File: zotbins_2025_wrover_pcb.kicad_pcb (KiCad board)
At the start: 2 copper layers, 125 x 125 mm, 40 parts, among them J1 FFC2B28-24-G, J2 DCJ200-10-A-XX-K_REVA, J6 Conn_01x30_Pin, U2 MCP23017_SP, U3 XC6206P302MR-G, U4 XC6206P282PR-G, U5 LM7805_TO220, U6 ESP32-DEVKITC-32D

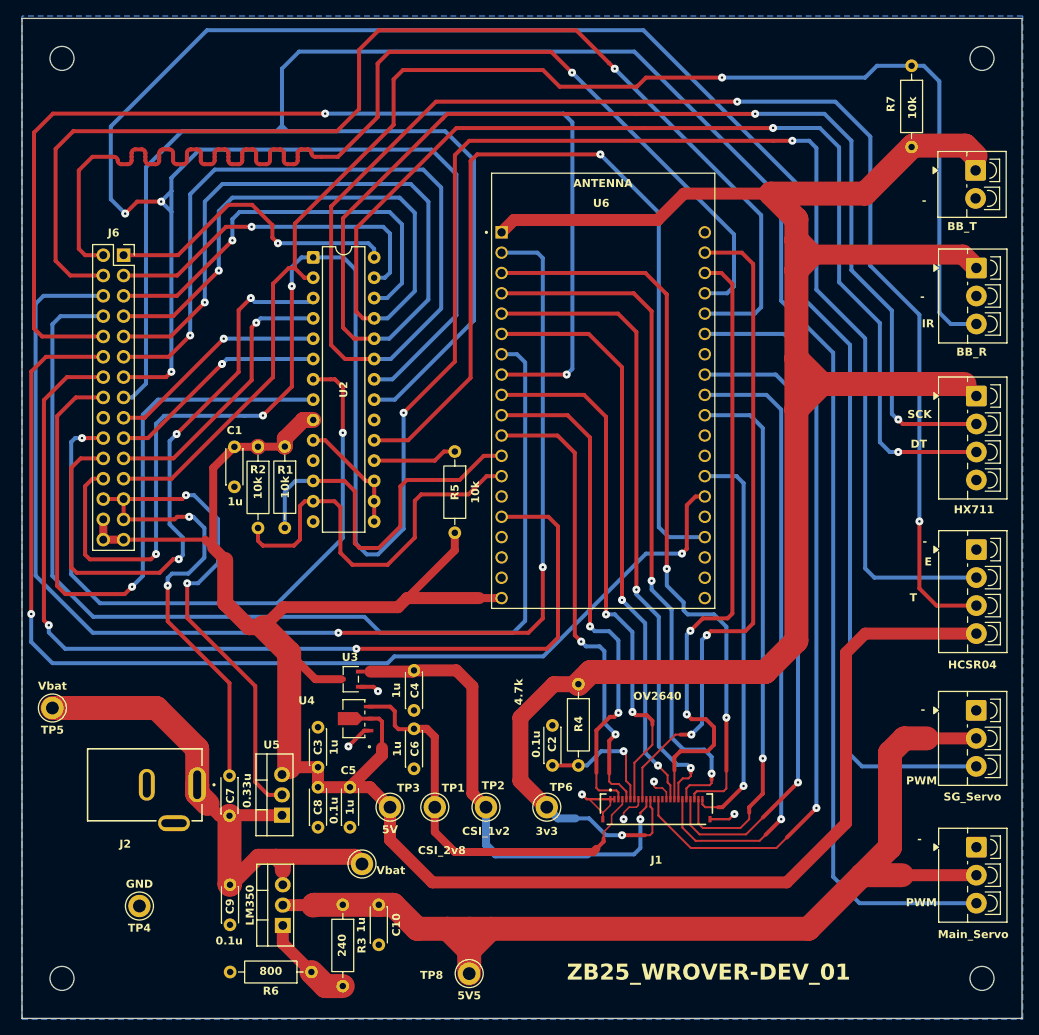
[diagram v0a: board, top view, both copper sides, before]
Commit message: hx711 bug update -- Digikey vendor sells different version of hx711 -> updated schematic + footprint
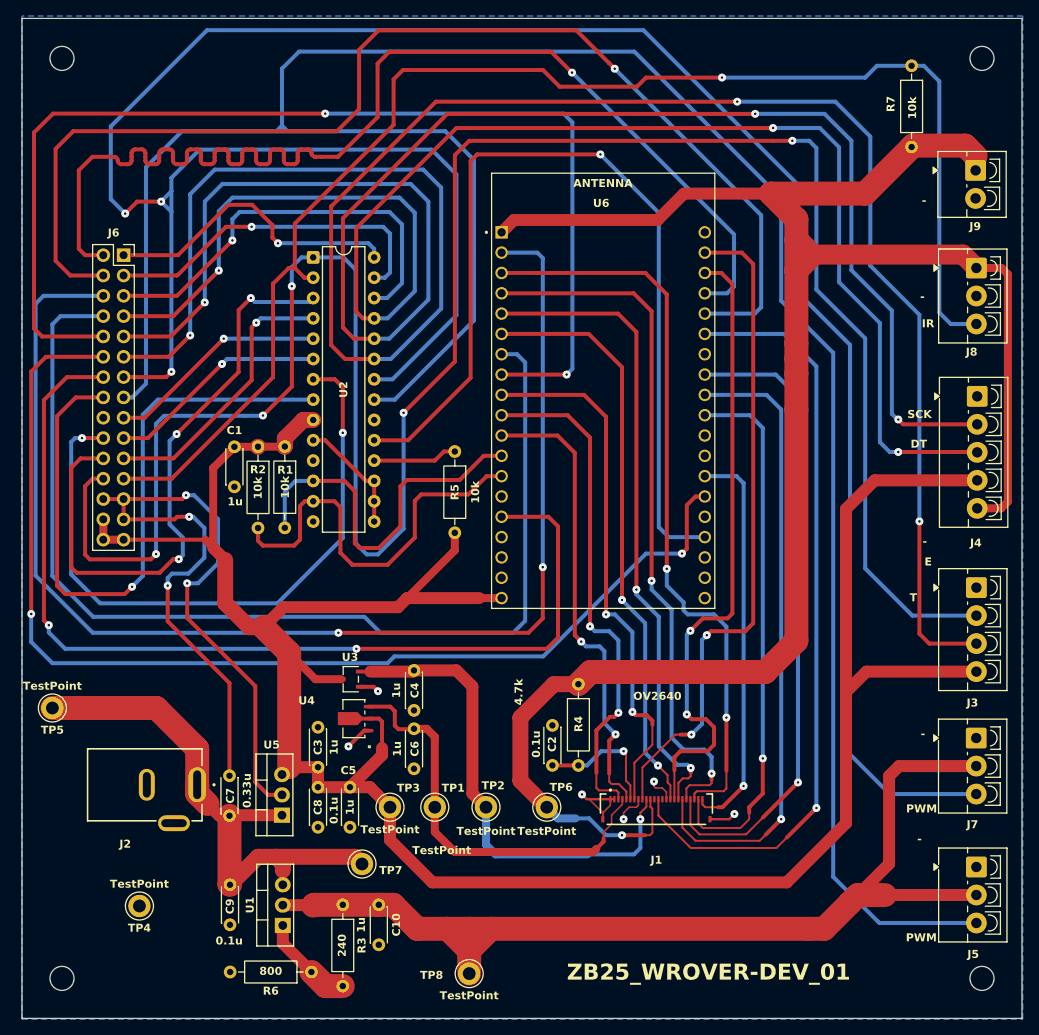
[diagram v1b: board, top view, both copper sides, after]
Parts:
- removed HX711: HX711_Screw_Terminal_01x04, TerminalBlock_4Ucon:TerminalBlock_4Ucon_1x04_P3.50mm_Vertical
- added J4: HX711_Screw_Terminal_01x05, TerminalBlock_4Ucon:TerminalBlock_4Ucon_1x05_P3.50mm_Vertical, F.Cu at (212.4, 84.6)
- TP1: value CSI_2v8 -> TestPoint
- TP2: value CSI_1v2 -> TestPoint
- TP3: value 5V -> TestPoint
- TP4: value GND -> TestPoint
- TP5: value Vbat -> TestPoint
- TP6: value 3v3 -> TestPoint
- TP8: value 5V5 -> TestPoint
- moved J3 4.75 mm to (212.3, 108.6)
- moved J7 3.46 mm to (212.3, 127.4)
- moved J5 2.48 mm to (212.3, 143.5)
- renumbered HCSR04 to J3, Main_Servo to J5, SG_Servo to J7, BB_R to J8, BB_T to J9, Vbat to TP7, LM350 to U1
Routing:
- net +5V: track 258.6 -> 294.5 mm
- net +3V3: track 249.1 -> 257.0 mm
- net /TRIG: track 251.7 -> 257.0 mm
- net /ECHO: track 287.1 -> 289.0 mm
- net /SG_SERVO_PWM: track 309.6 -> 311.0 mm
- net +5V5: track 132.2 -> 130.8 mm
- net /MAIN_SERVO_PWM: track 298.9 -> 300.0 mm

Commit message: completed PCB changes for iteration 2
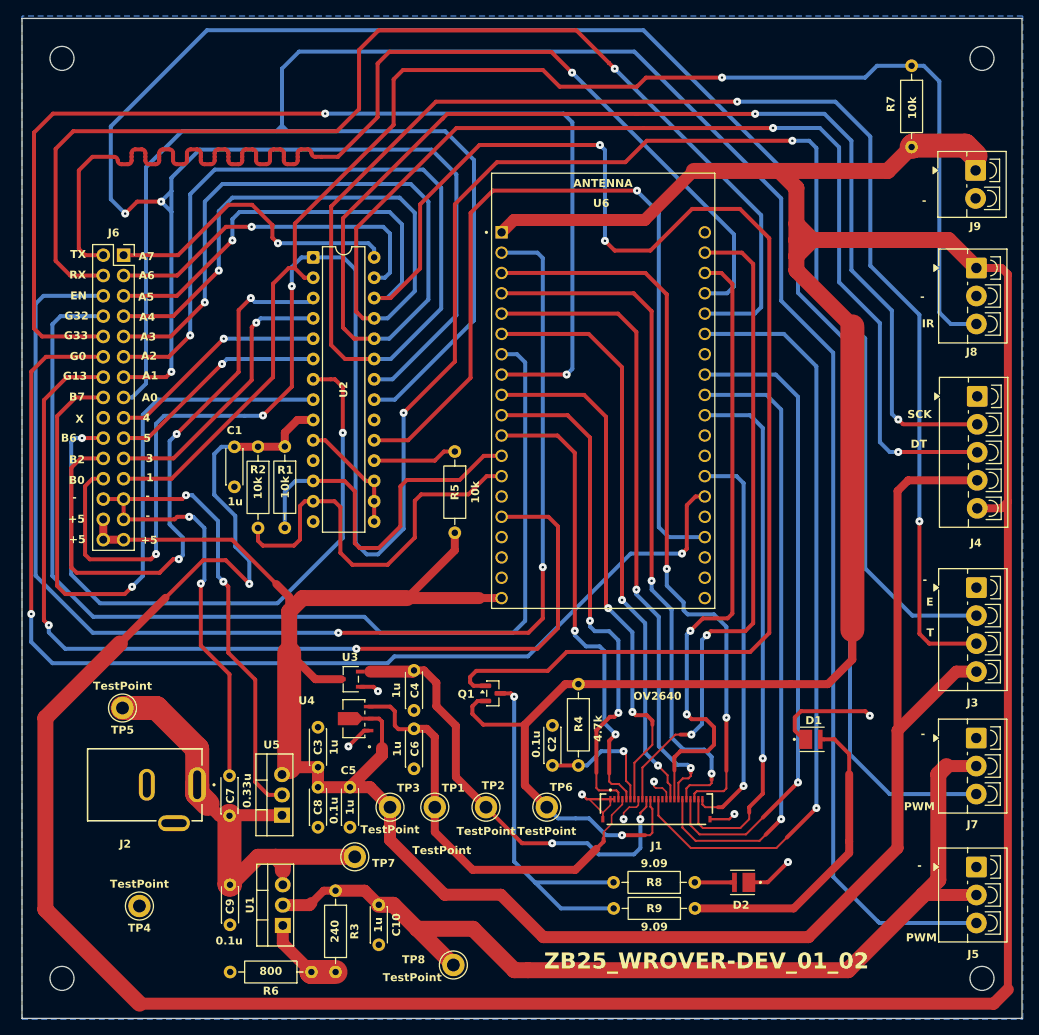
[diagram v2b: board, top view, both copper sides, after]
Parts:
- added D1: MP-3030-120H-30-95, LED:LED_MP-3030-120H-30-95, F.Cu at (191.8, 127.5)
- added D2: MP-3030-120H-30-95, LED:LED_MP-3030-120H-30-95, F.Cu at (183.1, 145.4)
- added Q1: IRLML9301, Package_TO_SOT_SMD:SOT-23, F.Cu at (151.9, 121.8)
- added R8: 9.09, Resistor_THT:R_Axial_DIN0207_L6.3mm_D2.5mm_P10.16mm_Horizontal, F.Cu at (177.1, 145.4)
- added R9: 9.09, Resistor_THT:R_Axial_DIN0207_L6.3mm_D2.5mm_P10.16mm_Horizontal, F.Cu at (177.1, 148.7)
- moved TP5 8.76 mm to (105.6, 123.6)
- moved TP8 2.25 mm to (146.9, 155.7)
- moved R3 1.98 mm to (132.2, 146.4)
- moved TP7 1.27 mm to (134.6, 142.2)
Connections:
- net /GPA5 renamed /~{LED}
- C1 pad 1: +5V -> +3V3
- R1 pad 1: +5V -> +3V3
- R2 pad 1: +5V -> +3V3
- U2 pad 9: +5V -> +3V3
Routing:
- net +3V3: track 257.0 -> 561.3 mm, vias 1 -> 2
- net /~{LED}: track 52.8 -> 222.4 mm, vias 1 -> 3
- net Net-(Q1-D): track 0.00 -> 47.2 mm, vias 0 -> 1
- net Net-(D1-PadA): track 0.00 -> 38.9 mm
- net +5V: track 294.5 -> 270.1 mm
- net GND: track 150.0 -> 160.6 mm, vias 10 -> 12
- net Net-(U1-VI): track 69.3 -> 59.3 mm
- net +5V5: track 130.8 -> 122.9 mm
- net /MCP_INTB: track 114.8 -> 107.3 mm
- net CSI_1V2: track 60.7 -> 55.6 mm, vias 1 -> 2
- net Net-(D2-PadA): track 0.00 -> 4.96 mm
- net /ECHO: track 289.0 -> 285.4 mm
- net CSI_2V8: track 51.3 -> 53.1 mm
- net Net-(U1-ADJ): track 12.0 -> 10.3 mm
- net /GPIO13: track 124.4 -> 123.7 mm
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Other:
- board text added: "ZB25_WROVER-DEV_01_02"
- board text removed: "V"
- board text removed: "ZB25_WROVER-DEV_01"

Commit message: minor adjustments + gerber files produced
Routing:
- net +3V3: track 561.3 -> 577.0 mm
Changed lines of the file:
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@@
 			(sketchdnponfab yes)
 			(crossoutdnponfab yes)
-			(subtractmaskfromsilk no)
+			(subtractmaskfromsilk yes)
 			(outputformat 1)
 			(mirror no)
@@
 	)
 	(segment
-		(start 131.642429 78.239717)
-		(end 131.642429 60.908968)
+		(start 205.179437 100.273394)
+		(end 205.179437 114.318387)
 		(width 0.5)
 		(layer "F.Cu")
@@
 	)
 	(segment
-		(start 205.179437 100.273394)
-		(end 205.179437 114.318387)
+		(start 205.179437 114.318387)
+		(end 206.412623 115.551573)
 		(width 0.5)
 		(layer "F.Cu")
@@
 	)
 	(segment
-		(start 131.642429 60.908968)
-		(end 144.741579 47.809818)
+		(start 133.377712 79.975)
+		(end 137.02 79.975)
 		(width 0.5)
 		(layer "F.Cu")
@@
 	)
 	(segment
-		(start 205.179437 114.318387)
-		(end 206.412623 115.551573)
+		(start 206.412623 115.551573)
+		(end 212.3 115.551573)
 		(width 0.5)
 		(layer "F.Cu")
@@
 	)
 	(segment
-		(start 144.741579 47.809818)
-		(end 182.405062 47.809818)
+		(start 114.025 77.025)
+		(end 111.35 79.7)
 		(width 0.5)
 		(layer "F.Cu")
@@
 	)
 	(segment
-		(start 206.412623 115.551573)
-		(end 212.3 115.551573)
+		(start 183.070342 47.809976)
+		(end 183.070184 47.809818)
 		(width 0.5)
 		(layer "F.Cu")
@@
 	)
 	(segment
-		(start 114.025 77.025)
-		(end 111.35 79.7)
+		(start 131.642429 60.908968)
+		(end 131.642429 78.239717)
 		(width 0.5)
 		(layer "F.Cu")
@@
 	)
 	(segment
-		(start 137.02 79.975)
-		(end 133.377712 79.975)
+		(start 183.070184 47.809818)
+		(end 144.741579 47.809818)
 		(width 0.5)
 		(layer "F.Cu")
@@
 	)
 	(segment
-		(start 133.377712 79.975)
-		(end 131.642429 78.239717)
+		(start 131.642429 78.239717)
+		(end 133.377712 79.975)
 		(width 0.5)
 		(layer "F.Cu")
@@
 		(net 25)
 	)
+	(segment
+		(start 144.741579 47.809818)
+		(end 131.642429 60.908968)
+		(width 0.5)
+		(layer "F.Cu")
+		(net 25)
+	)
 	(via
 		(at 205.177816 100.271773)
@@
 	)
 	(via
-		(at 182.405062 47.809818)
+		(at 183.070342 47.809976)
 		(size 1)
 		(drill 0.3)
@@
 	)
 	(segment
-		(start 182.405062 47.809818)
-		(end 194.675487 47.809818)
+		(start 199.04094 68.30805)
+		(end 205.177816 74.444926)
 		(width 0.5)
 		(layer "B.Cu")
@@
 	)
 	(segment
-		(start 194.675487 47.809818)
-		(end 199.04094 52.175271)
+		(start 205.177816 74.444926)
+		(end 205.177816 100.271773)
 		(width 0.5)
 		(layer "B.Cu")
@@
 	)
 	(segment
-		(start 199.04094 52.175271)
-		(end 199.04094 68.30805)
+		(start 143.15 56.3)
+		(end 145.4 58.55)
 		(width 0.5)
 		(layer "B.Cu")
@@
 	)
 	(segment
-		(start 143.15 56.3)
-		(end 145.4 58.55)
+		(start 114.025 77.025)
+		(end 114.025 59.375)
 		(width 0.5)
 		(layer "B.Cu")
@@
 	)
 	(segment
-		(start 114.025 77.025)
-		(end 114.025 59.375)
+		(start 194.675645 47.809976)
+		(end 199.04094 52.175271)
 		(width 0.5)
 		(layer "B.Cu")
@@
 	)
 	(segment
-		(start 199.04094 68.30805)
-		(end 205.177816 74.444926)
+		(start 183.070342 47.809976)
+		(end 194.675645 47.809976)
 		(width 0.5)
 		(layer "B.Cu")
@@
 	)
 	(segment
-		(start 205.177816 74.444926)
-		(end 205.177816 100.271773)
+		(start 199.04094 52.175271)
+		(end 199.04094 68.30805)
 		(width 0.5)
 		(layer "B.Cu")
@@
 	)
 	(segment
+		(start 189.291237 52.694359)
+		(end 171.097037 52.694359)
+		(width 0.5)
+		(layer "F.Cu")
+		(net 26)
+	)
+	(segment
 		(start 100.885425 95.868707)
 		(end 101.814132 94.94)
@@
 	)
 	(segment
-		(start 152.359682 55.377846)
-		(end 147.113266 60.624262)
+		(start 168.41355 55.377846)
+		(end 152.359682 55.377846)
 		(width 0.5)
 		(layer "F.Cu")
@@
 	)
 	(segment
-		(start 147.113266 80.286734)
-		(end 140.7 86.7)
+		(start 152.359682 55.377846)
+		(end 147.113266 60.624262)
 		(width 0.5)
 		(layer "F.Cu")
@@
 	)
 	(segment
+		(start 147.113266 60.624262)
+		(end 147.113266 80.286734)
+		(width 0.5)
+		(layer "F.Cu")
+		(net 26)
+	)
+	(segment
 		(start 126.733259 77.545184)
 		(end 126.733259 70.885526)
@@
 	)
 	(segment
-		(start 101.475983 105.017742)
-		(end 109.097872 105.017742)
+		(start 171.097037 52.694359)
+		(end 168.41355 55.377846)
 		(width 0.5)
 		(layer "F.Cu")
@@
 	)
 	(segment
-		(start 101.814132 94.94)
-		(end 103.16 94.94)
+		(start 101.475983 105.017742)
+		(end 109.097872 105.017742)
 		(width 0.5)
 		(layer "F.Cu")
@@
 	)
 	(segment
-		(start 171.097037 52.694359)
-		(end 168.41355 55.377846)
+		(start 101.814132 94.94)
+		(end 103.16 94.94)
 		(width 0.5)
 		(layer "F.Cu")
@@
 	)
 	(segment
-		(start 147.113266 60.624262)
-		(end 147.113266 80.286734)
+		(start 147.113266 80.286734)
+		(end 140.7 86.7)
 		(width 0.5)
 		(layer "F.Cu")
@@
 	)
 	(segment
-		(start 189.291237 52.694359)
-		(end 171.097037 52.694359)
-		(width 0.5)
-		(layer "F.Cu")
-		(net 26)
-	)
-	(segment
 		(start 126.733259 83.426723)
 		(end 126.733259 77.545184)
@@
 		(net 26)
 	)
-	(segment
-		(start 168.41355 55.377846)
-		(end 152.359682 55.377846)
-		(width 0.5)
-		(layer "F.Cu")
-		(net 26)
-	)
 	(via
 		(at 123.121499 87.038483)
@@
 	)
 	(segment
-		(start 204.301573 112.051573)
-		(end 212.3 112.051573)
+		(start 198.4 106.15)
+		(end 204.301573 112.051573)
 		(width 0.5)
 		(layer "B.Cu")
@@
 	)
 	(segment
-		(start 198.4 77.4)
-		(end 198.4 106.15)
+		(start 134.7 103)
+		(end 134.7 68.8)
 		(width 0.5)
 		(layer "B.Cu")
@@
 	)
 	(segment
-		(start 198.4 106.15)
-		(end 204.301573 112.051573)
+		(start 127.936343 67.275)
+		(end 129.4 67.275)
 		(width 0.5)
 		(layer "B.Cu")
@@
 	)
 	(segment
-		(start 189.291237 52.694359)
-		(end 191.394359 52.694359)
+		(start 110.753705 87.075686)
+		(end 109.7561 88.073291)
 		(width 0.5)
 		(layer "B.Cu")
@@
 	)
 	(segment
-		(start 191.394359 52.694359)
-		(end 192.3 53.6)
+		(start 192.3 53.6)
+		(end 192.3 71.3)
 		(width 0.5)
 		(layer "B.Cu")
@@
 	)
 	(segment
-		(start 134.7 103)
-		(end 134.7 68.8)
+		(start 189.291237 52.694359)
+		(end 191.394359 52.694359)
 		(width 0.5)
 		(layer "B.Cu")
@@
 	)
 	(segment
-		(start 127.936343 67.275)
-		(end 129.4 67.275)
+		(start 140.7 101.2)
+		(end 137.5 104.4)
 		(width 0.5)
 		(layer "B.Cu")
@@
 	)
 	(segment
-		(start 110.753705 87.075686)
-		(end 109.7561 88.073291)
+		(start 120.864053 87.075686)
+		(end 123.084296 87.075686)
 		(width 0.5)
 		(layer "B.Cu")
@@
 	)
 	(segment
-		(start 140.7 101.2)
-		(end 137.5 104.4)
+		(start 191.394359 52.694359)
+		(end 192.3 53.6)
 		(width 0.5)
 		(layer "B.Cu")
@@
 	)
 	(segment
-		(start 120.864053 87.075686)
-		(end 123.084296 87.075686)
+		(start 123.084296 87.075686)
+		(end 123.121499 87.038483)
 		(width 0.5)
 		(layer "B.Cu")
@@
 	)
 	(segment
-		(start 123.084296 87.075686)
-		(end 123.121499 87.038483)
+		(start 198.4 77.4)
+		(end 198.4 106.15)
 		(width 0.5)
 		(layer "B.Cu")
@@
 	)
 	(segment
-		(start 192.3 53.6)
-		(end 192.3 71.3)
+		(start 204.301573 112.051573)
+		(end 212.3 112.051573)
 		(width 0.5)
 		(layer "B.Cu")
@@
 	)
 	(segment
+		(start 212.2 56.4)
+		(end 214.029855 56.4)
+		(width 1)
+		(layer "F.Cu")
+		(net 48)
+	)
+	(segment
 		(start 170.9 139.5)
 		(end 171.5 139.5)
@@
 		(width 1)
 		(layer "F.Cu")
+		(net 48)
+	)
+	(segment
+		(start 214.029855 56.4)
+		(end 216.236088 58.606233)
+		(width 1)
+		(layer "F.Cu")
+		(net 48)
+	)
+	(segment
+		(start 216.236088 58.606233)
+		(end 216.236088 69.39416)
+		(width 1)
+		(layer "F.Cu")

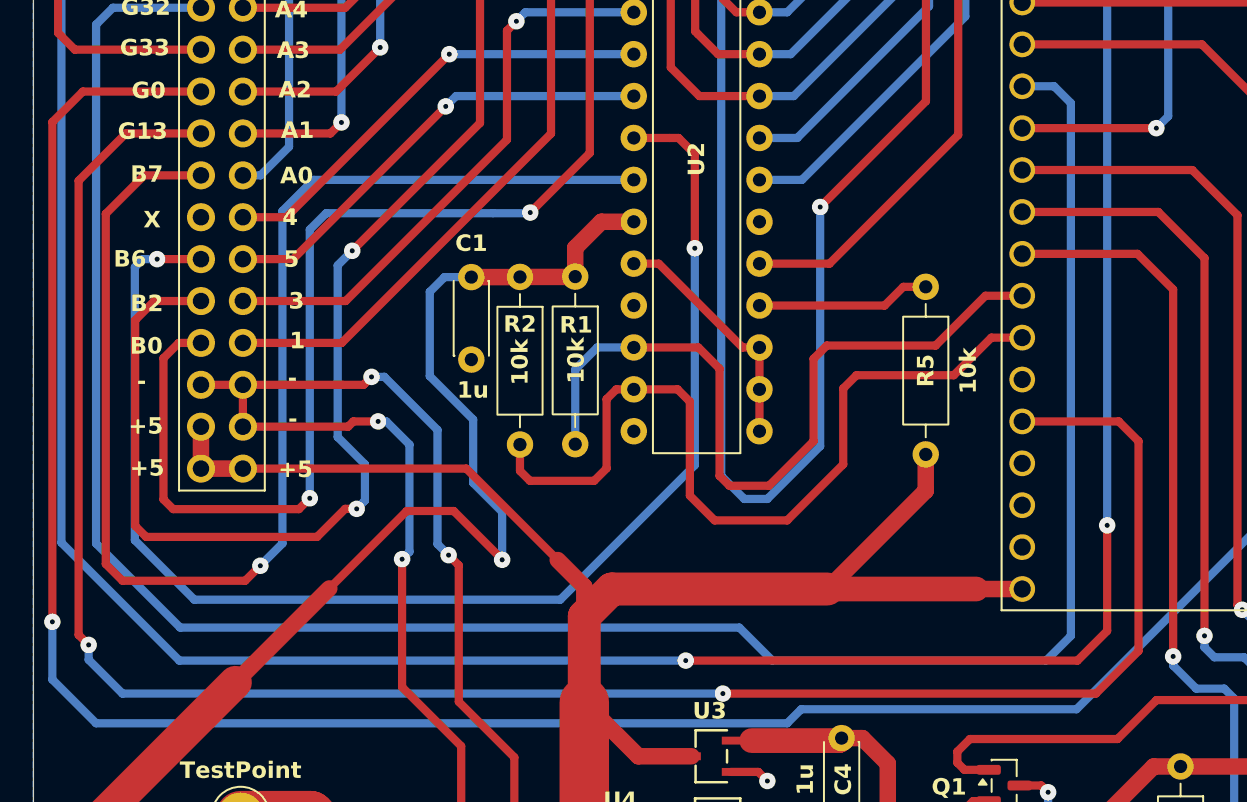
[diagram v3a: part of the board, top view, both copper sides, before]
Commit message: fixed GPIO issue within gpio expander
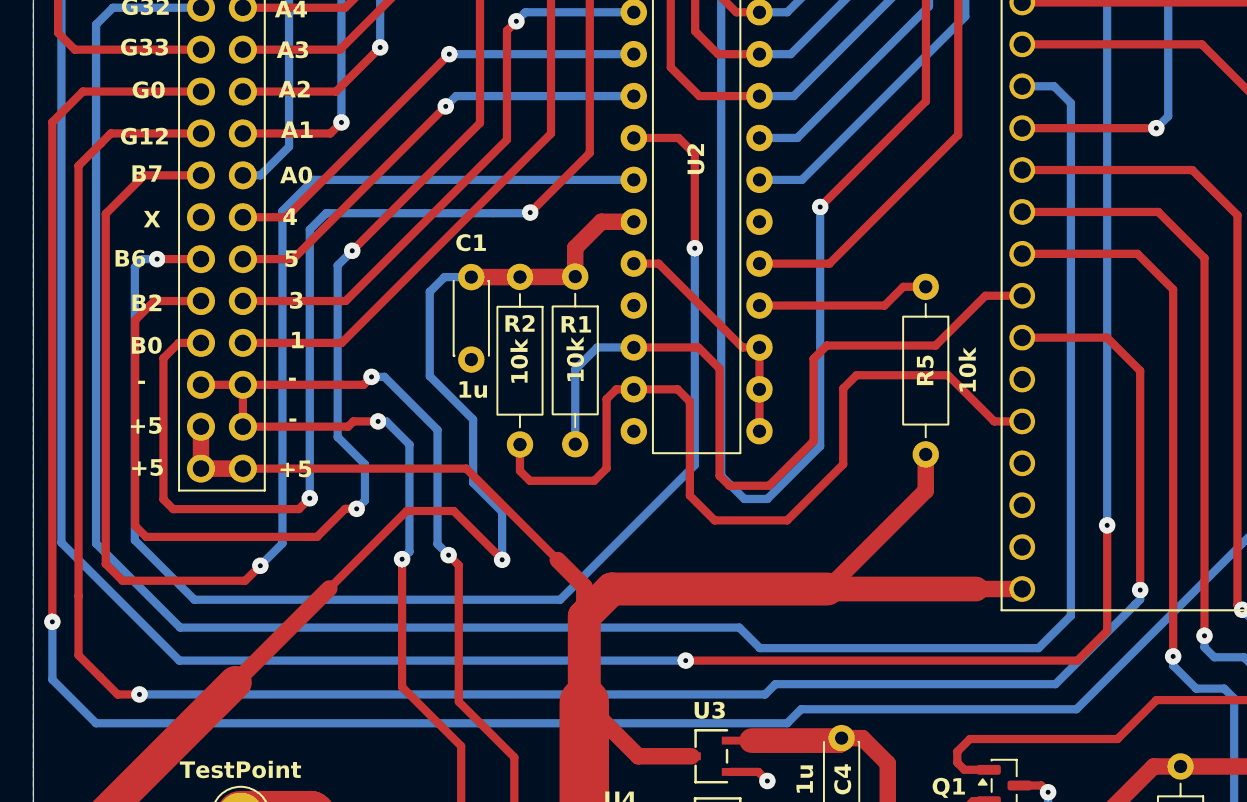
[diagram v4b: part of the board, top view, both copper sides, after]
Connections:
- J6 pad 14: /GPIO13 -> /GPIO_12
- U6 pad J2-13: /GPIO_SCK -> /GPIO_12
- U6 pad J2-15: /GPIO13 -> /GPIO_SCK
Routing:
- net /GPIO_12: track 0.00 -> 127.5 mm, vias 0 -> 2
- net /GPIO13: track 123.7 -> 0.00 mm, vias 2 -> 0
- net /GPIO32: track 136.6 -> 135.2 mm
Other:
- board text added: "G12"
- board text removed: "G13"

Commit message: iteration 2 modified, components changed
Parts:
- removed D1, D2: MP-3030-120H-30-95, LED:LED_MP-3030-120H-30-95
- removed Q1: IRLML9301, Package_TO_SOT_SMD:SOT-23
- removed R8, R9: 9.09, Resistor_THT:R_Axial_DIN0207_L6.3mm_D2.5mm_P10.16mm_Horizontal
- J1: value FFC2B28-24-G -> Conn_01x28_Pin; footprint Library:GCT_FFC2B28-24-G -> Connector_FFC-FPC:TE_2-84953-8_1x28-1MP_P1.0mm_Horizontal
- moved TP6 101.6 mm to (213.0, 50.2)
- moved C2 39.5 mm to (196.8, 143.4), turned to -90 degrees
- moved R4 35.7 mm to (196.8, 130.7)
- moved J1 1.88 mm to (172.9, 134.5)
- moved TP2 0.90 mm to (150.1, 136.2)
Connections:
- J1 pad 1: GND -> /STROBE
- J1 pad 15: GND -> /DGND
- J1 pad 2: GND -> /AGND
- J1 pad 8: GND -> /PWDN
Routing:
- net Net-(Q1-D): track 47.2 -> 0.00 mm, vias 1 -> 0
- net Net-(D1-PadA): track 38.9 -> 0.00 mm
- net /RESETB: track 16.0 -> 48.3 mm, vias 1 -> 0
- net +3V3: track 577.0 -> 544.9 mm, vias 2 -> 1
- net GND: track 160.6 -> 128.7 mm, vias 12 -> 7
- net /~{LED}: track 222.4 -> 197.5 mm
- net /DATA1: track 67.6 -> 54.2 mm
- net CSI_1V2: track 55.6 -> 66.6 mm, vias 2 -> 1
- net /DATA4: track 93.5 -> 85.3 mm, vias 2 -> 0
- net /SIOD: track 63.8 -> 56.2 mm, vias 2 -> 0
- net /XCLK1: track 96.4 -> 104.0 mm
- net /DATA0: track 50.1 -> 42.7 mm
- net /HREF: track 83.0 -> 75.6 mm
- net /DATA5: track 88.1 -> 81.1 mm, vias 2 -> 0
- net /SIOC: track 58.2 -> 51.6 mm
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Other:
- board text added: "+3V3"
- board text added: "+5V"
